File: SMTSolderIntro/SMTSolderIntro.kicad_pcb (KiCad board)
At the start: 2 copper layers, 88.9 x 63.5 mm, 149 parts, among them J1 USB_C_PWR_THRU, J2 Barrel_Jack, U1 NE556, U2 M74LCX04, U3 NE556

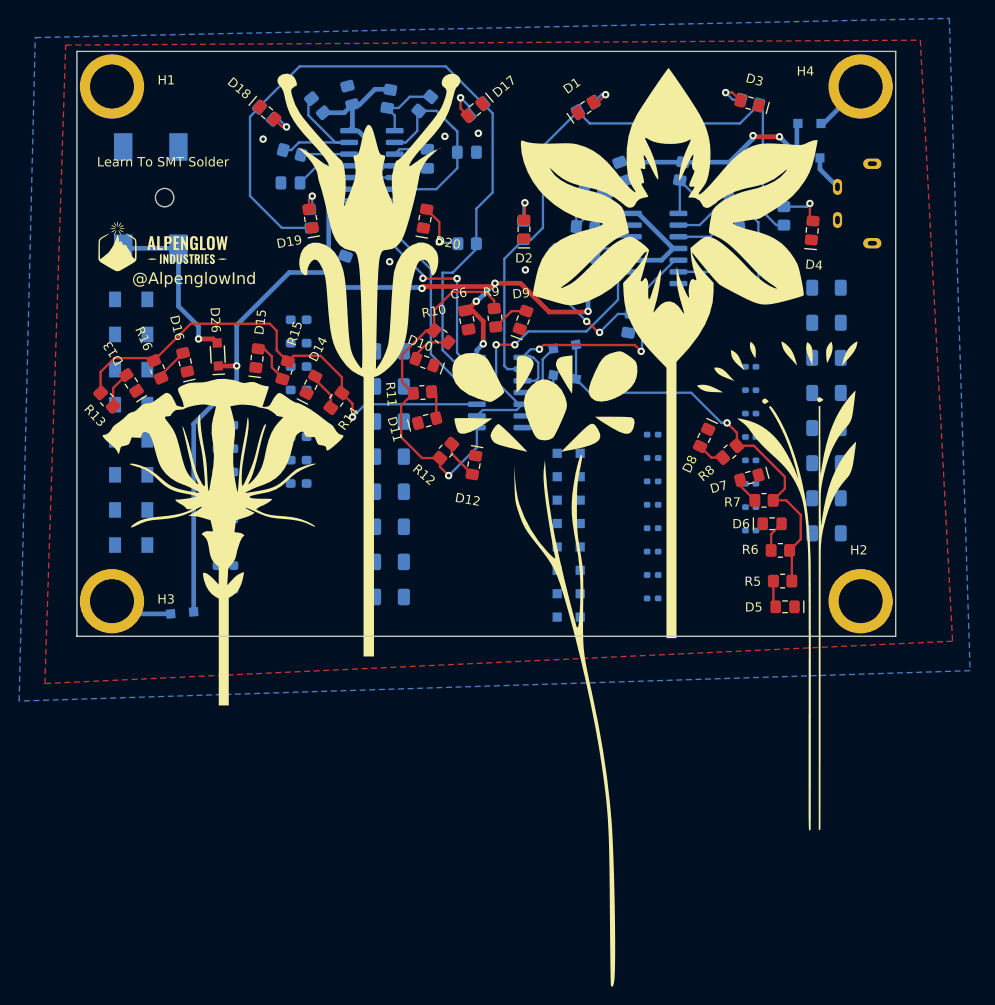
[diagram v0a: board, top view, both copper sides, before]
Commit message: Updated layout, Labeled practice component sizes, Added board name, Updated Schematic
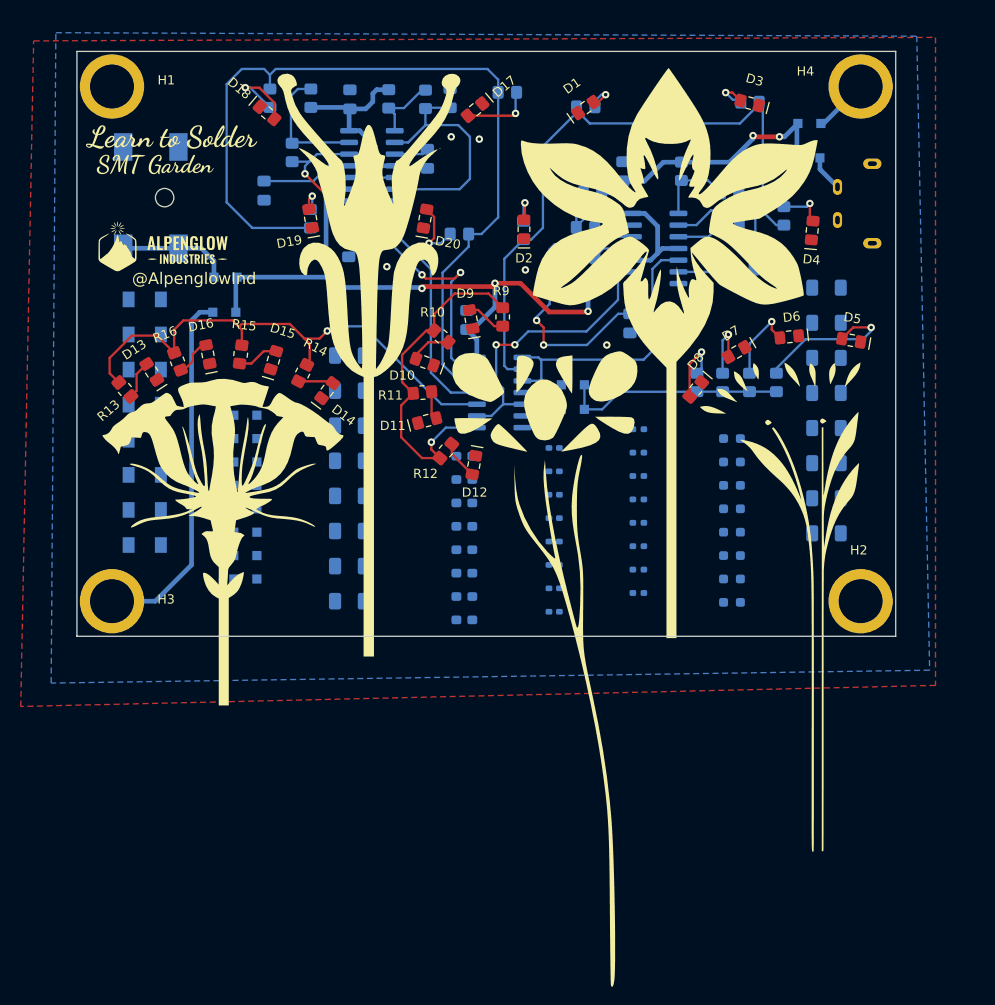
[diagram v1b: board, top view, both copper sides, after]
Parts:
- added G***: LOGO, Alpenglow_SMT_Soldering_PCB:LearnToSolderDancing20mm, F.Cu at (124.7, 59.0)
- added G***: LOGO, Alpenglow_SMT_Soldering_PCB:SMTGardenDancing15mm, F.Cu at (123.3, 60.9)
- C6, D26, R5, R6, R7, R8: moved to B.Cu
- moved R37 55.0 mm to (185.4, 87.8)
- moved R38 55.0 mm to (185.4, 90.3)
- moved R39 55.0 mm to (185.4, 92.8)
- moved R40 55.0 mm to (185.4, 95.4)
- moved R41 55.0 mm to (185.4, 97.9)
- moved R42 55.0 mm to (185.4, 100.5)
- moved R43 55.0 mm to (185.4, 103.0)
- moved R44 55.0 mm to (185.4, 105.5)
- moved D27 35.4 mm to (132.6, 85.2)
- moved D28 35.4 mm to (132.6, 87.8)
- moved D29 35.4 mm to (132.6, 90.3)
- moved D30 35.4 mm to (132.6, 92.8)
- moved D31 35.4 mm to (132.6, 95.4)
- moved D32 35.4 mm to (132.6, 97.9)
- moved D33 35.4 mm to (132.6, 100.5)
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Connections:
- C16 pad 2: unconnected-(C16-Pad2) -> GND
- C17 pad 2: unconnected-(C17-Pad2) -> GND
- C18 pad 2: unconnected-(C18-Pad2) -> GND
- C19 pad 2: unconnected-(C19-Pad2) -> GND
- C24 pad 2: unconnected-(C24-Pad2) -> GND
- C25 pad 2: unconnected-(C25-Pad2) -> GND
- C26 pad 2: unconnected-(C26-Pad2) -> GND
- C27 pad 2: unconnected-(C27-Pad2) -> GND
- C32 pad 2: unconnected-(C32-Pad2) -> GND
- C33 pad 2: unconnected-(C33-Pad2) -> GND
- C34 pad 2: unconnected-(C34-Pad2) -> GND
- C35 pad 2: unconnected-(C35-Pad2) -> GND
- D31 pad A: unconnected-(D31-PadA) -> GND
- D32 pad A: unconnected-(D32-PadA) -> GND
- D33 pad A: unconnected-(D33-PadA) -> GND
- D34 pad A: unconnected-(D34-PadA) -> GND
- D39 pad A: unconnected-(D39-PadA) -> GND
- D40 pad A: unconnected-(D40-PadA) -> GND
- D41 pad A: unconnected-(D41-PadA) -> GND
- D42 pad A: unconnected-(D42-PadA) -> GND
- R33 pad 2: unconnected-(R33-Pad2) -> GND
- R34 pad 2: unconnected-(R34-Pad2) -> GND
- R35 pad 2: unconnected-(R35-Pad2) -> GND
- R36 pad 2: unconnected-(R36-Pad2) -> GND
- R41 pad 2: unconnected-(R41-Pad2) -> GND
- R42 pad 2: unconnected-(R42-Pad2) -> GND
- R43 pad 2: unconnected-(R43-Pad2) -> GND
- R44 pad 2: unconnected-(R44-Pad2) -> GND
- R49 pad 2: unconnected-(R49-Pad2) -> GND
- R50 pad 2: unconnected-(R50-Pad2) -> GND
- R51 pad 2: unconnected-(R51-Pad2) -> GND
- R52 pad 2: unconnected-(R52-Pad2) -> GND
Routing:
- net +Vin_1: track 6.95 -> 39.5 mm
- net +5V: track 176.0 -> 144.1 mm, vias 8 -> 5
- net /BLINK5: track 46.1 -> 24.3 mm, vias 1 -> 0
- net Net-(D5-PadA): track 2.89 -> 16.5 mm, vias 0 -> 1
- net /BLINK4: track 81.1 -> 94.5 mm
- net +Vbarrel: track 18.9 -> 12.2 mm, vias 1 -> 0
- net Net-(C4-Pad1): track 29.4 -> 35.8 mm
- net Net-(D18-PadA): track 3.44 -> 9.14 mm
- net Net-(D6-PadA): track 3.36 -> 8.73 mm, vias 0 -> 1
- net Net-(C8-Pad1): track 22.1 -> 27.2 mm
- net Net-(D8-PadA): track 2.96 -> 7.90 mm, vias 0 -> 1
- net /BLINK3: track 53.9 -> 58.1 mm
- net Net-(D7-PadA): track 2.85 -> 6.89 mm, vias 0 -> 1
- net Net-(C11-Pad1): track 6.09 -> 9.92 mm
- net Net-(D17-PadA): track 4.60 -> 7.62 mm
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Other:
- board text added: "0402"
- board text added: "0603"
- board text added: "1206"
- board text added: "GND"
- board text added: "MINI-MELF"
- board text added: "SOD-323"
- board text removed: "Learn To SMT Solder"

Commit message: changed some practice area positions & text sizes
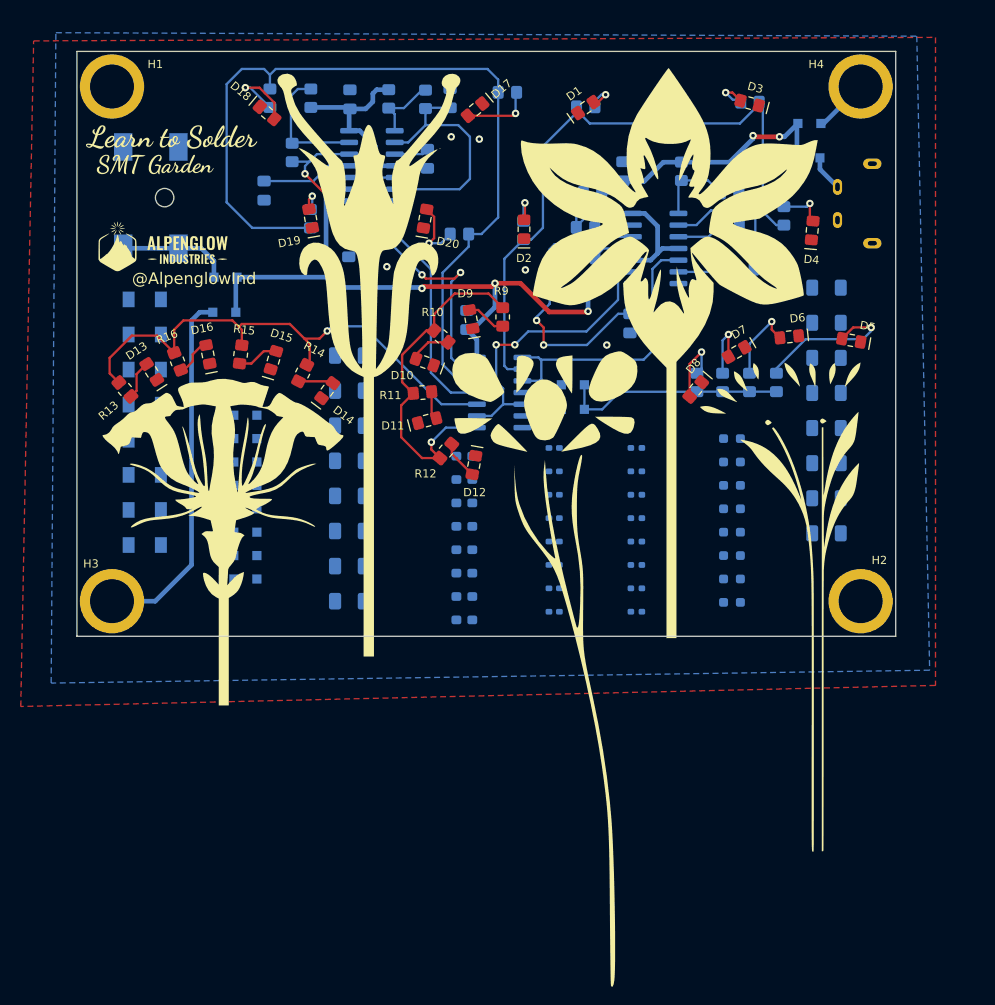
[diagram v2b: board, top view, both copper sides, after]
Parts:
- moved R49 2.04 mm to (175.0, 98.9)
- moved R51 2.04 mm to (175.0, 104.0)
- moved R45 2.04 mm to (175.0, 88.8)
- moved R46 2.04 mm to (175.0, 91.3)
- moved R47 2.04 mm to (175.0, 93.9)
- moved R48 2.04 mm to (175.0, 96.4)
- moved R50 2.04 mm to (175.0, 101.5)
- moved R52 2.04 mm to (175.0, 106.6)

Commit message: Moved practice resistors and capacitors, Added words on back
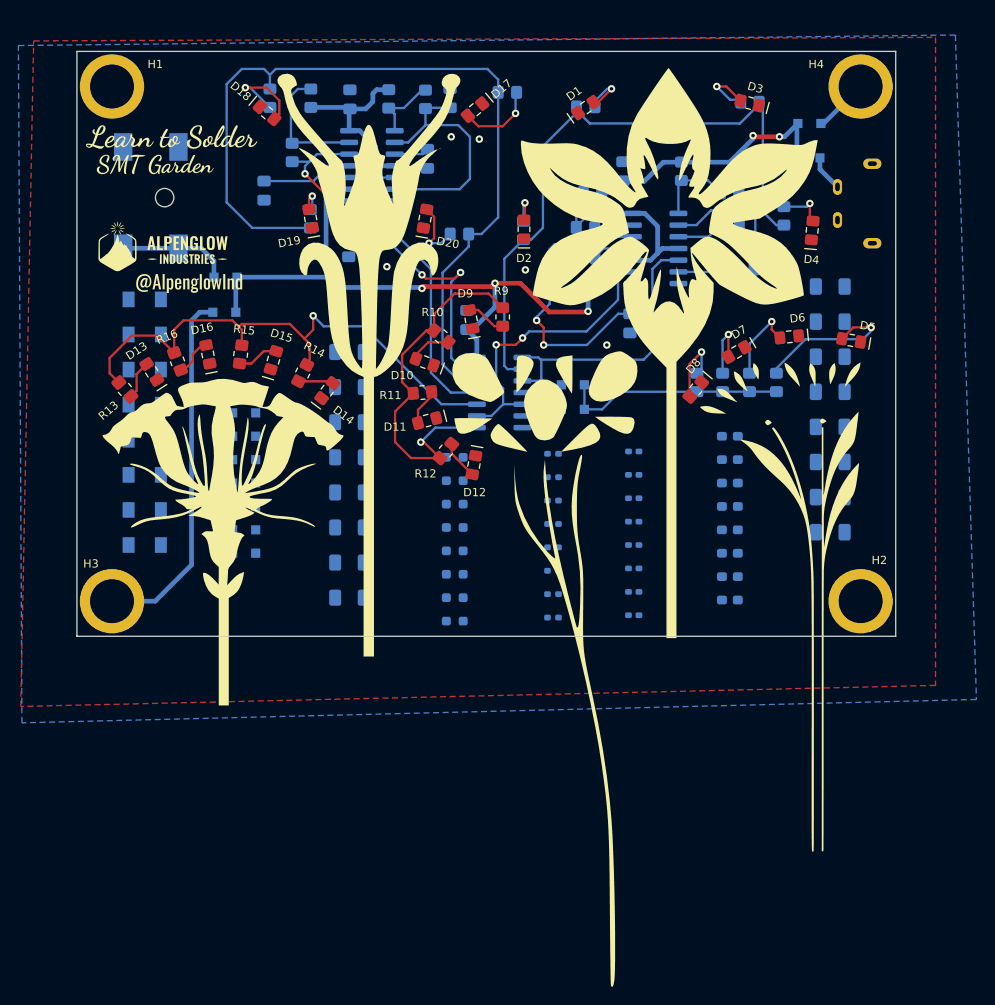
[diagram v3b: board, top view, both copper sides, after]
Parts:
- added G***: LOGO, Alpenglow_SMT_Soldering_PCB:SMTGardenCurvedDancing30mm, B.Cu at (156.2, 78.5)
- added G***: LOGO, Alpenglow_SMT_Soldering_PCB:PracticeStalksDancing20mm, B.Cu at (130.6, 108.3)
- added G***: LOGO, Alpenglow:@AlpenglowIndOswald20mm, F.Cu at (126.5, 73.9)
- moved C16 52.7 mm to (196.1, 86.5)
- moved C17 52.7 mm to (196.1, 90.3)
- moved C12 52.7 mm to (196.1, 71.2)
- moved C13 52.7 mm to (196.1, 75.1)
- moved C14 52.7 mm to (196.1, 78.9)
- moved C15 52.7 mm to (196.1, 82.7)
- moved C18 52.7 mm to (196.1, 94.1)
- moved C19 52.7 mm to (196.1, 97.9)
- moved R29 52.3 mm to (143.9, 78.4)
- moved R30 52.3 mm to (143.9, 82.2)
- moved R31 52.3 mm to (143.9, 86.0)
- moved R32 52.3 mm to (143.9, 89.8)
- moved R33 52.3 mm to (143.9, 93.6)
- moved R34 52.3 mm to (143.9, 97.4)
- moved R35 52.3 mm to (143.9, 101.2)
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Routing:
- net /BLINK2: track 38.2 -> 41.3 mm
- net Net-(D3-PadA): track 3.98 -> 6.45 mm
- net /BLINK3: track 58.1 -> 60.0 mm
- net Net-(D1-PadA): track 3.29 -> 5.08 mm
- net Net-(D17-PadA): track 7.62 -> 8.56 mm
- net Net-(D11-PadA): track 3.08 -> 4.01 mm
- net Net-(D18-PadA): track 9.14 -> 10.0 mm
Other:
- board text added: "C-0402"
- board text added: "C-0603"
- board text added: "C-1206"
- board text added: "DIODES"
- board text added: "R-0402"
- board text added: "R-0603"
- board text added: "R-1206"
- board text removed: "0402"
- board text removed: "0603"
- board text removed: "1206"
- board text removed: "@AlpenglowInd"

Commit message: spread out logo & text so more attention is on flowers
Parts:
- moved G*** 64.6 mm to (184.2, 102.9), turned to 90 degrees
- moved G*** 59.8 mm to (157.4, 110.1)
- moved G*** 58.7 mm to (156.8, 108.2)
- moved G*** 2.71 mm to (122.0, 64.8)
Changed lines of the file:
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@@
   )
   (footprint "Alpenglow:Alpenglow_Logo_Horiz_15x6.2" (layer "F.Cu")
-    (at 123.607772 66.989713)
+    (at 122.047 64.77)
     (attr board_only exclude_from_pos_files exclude_from_bom)
     (fp_text reference "G***" (at 0 0) (layer "F.SilkS") hide
@@
   )
   (footprint "Alpenglow_SMT_Soldering_PCB:SMTGardenDancing15mm" (layer "F.Cu")
-    (at 123.344432 60.91903)
+    (at 157.360131 110.054229)
     (attr board_only exclude_from_pos_files exclude_from_bom)
     (fp_text reference "G***" (at 0.000009 0.000004) (layer "F.SilkS") hide
@@
   )
   (footprint "Alpenglow:@AlpenglowIndOswald20mm" (layer "F.Cu")
-    (at 126.491585 73.874392)
+    (at 184.237392 102.870415 90)
     (attr board_only exclude_from_pos_files exclude_from_bom)
-    (fp_text reference "G***" (at 0 0) (layer "F.SilkS") hide
+    (fp_text reference "G***" (at 0 0 90) (layer "F.SilkS") hide
       (effects (font (size 1.524 1.524) (thickness 0.3)))
     )
-    (fp_text value "LOGO" (at 0.75 0) (layer "F.SilkS") hide
+    (fp_text value "LOGO" (at 0.75 0 90) (layer "F.SilkS") hide
       (effects (font (size 1.524 1.524) (thickness 0.3)))
     )
@@
   )
   (footprint "Alpenglow_SMT_Soldering_PCB:LearnToSolderDancing20mm" (layer "F.Cu")
-    (at 124.693708 59.041203)
+    (at 156.824708 108.190203)
     (attr board_only exclude_from_pos_files exclude_from_bom)
     (fp_text reference "G***" (at -0.000003 0.000005) (layer "F.SilkS") hide
@@
     (pts (xy 203.2 45.72) (xy 203.2 109.22))
     (height -5.08)
-    (gr_text "2500.0000 mils" (at 207.13 77.47 90) (layer "F.Fab")
+    (gr_text "2.5000 in" (at 207.13 77.47 90) (layer "F.Fab")
       (effects (font (size 1 1) (thickness 0.15)))
     )
@@
     (pts (xy 114.3 45.72) (xy 203.2 45.72))
     (height -5.08)
-    (gr_text "3500.0000 mils" (at 158.75 39.49) (layer "F.Fab")
+    (gr_text "3.5000 in" (at 158.75 39.49) (layer "F.Fab")
       (effects (font (size 1 1) (thickness 0.15)))
     )
